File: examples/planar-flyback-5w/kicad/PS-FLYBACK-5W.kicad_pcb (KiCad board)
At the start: 6 copper layers, 50 x 104 mm, 29 parts, among them J1 18-36 V DC, J2 5 V / 1 A isolated, T1 PLANAR 4:2 / Lm 13.12uH, U1 LT8302IS8E#PBF

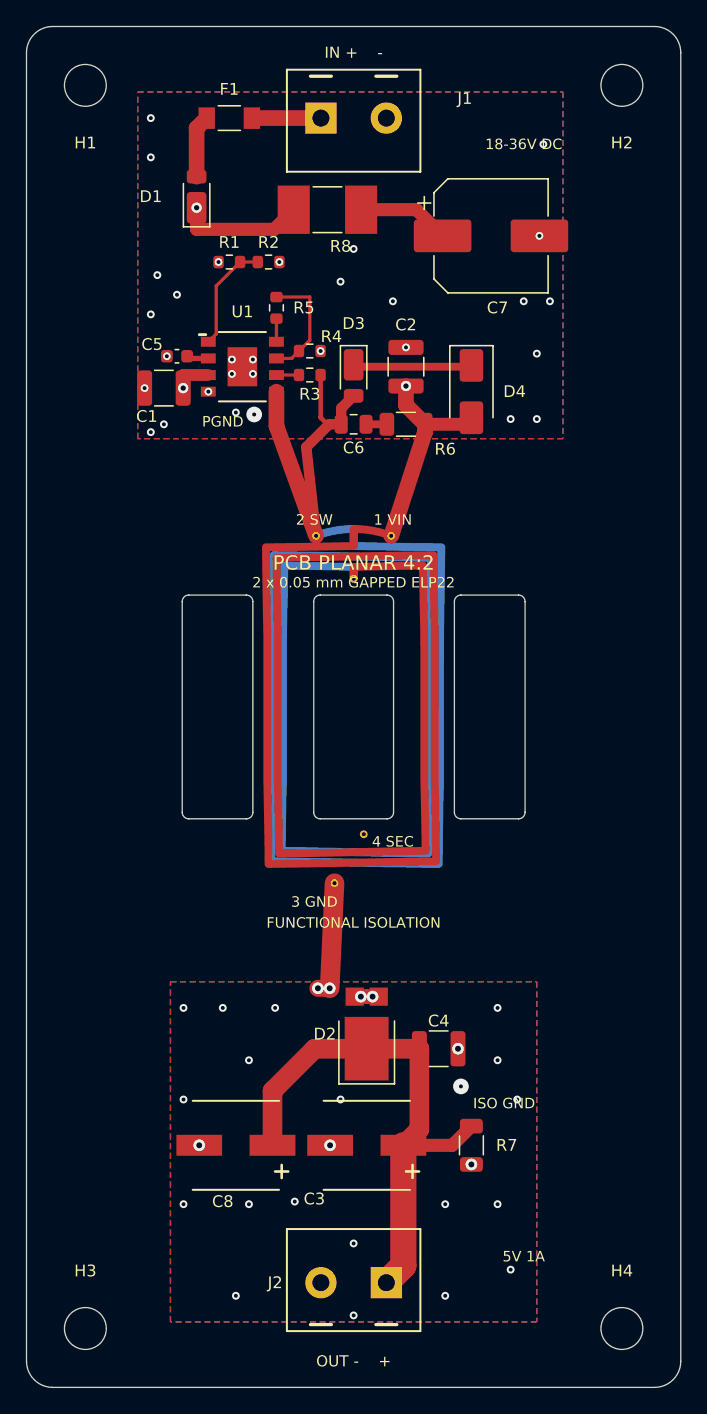
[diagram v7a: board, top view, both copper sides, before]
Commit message: Compact flyback A3 and verify TDK clip clearance
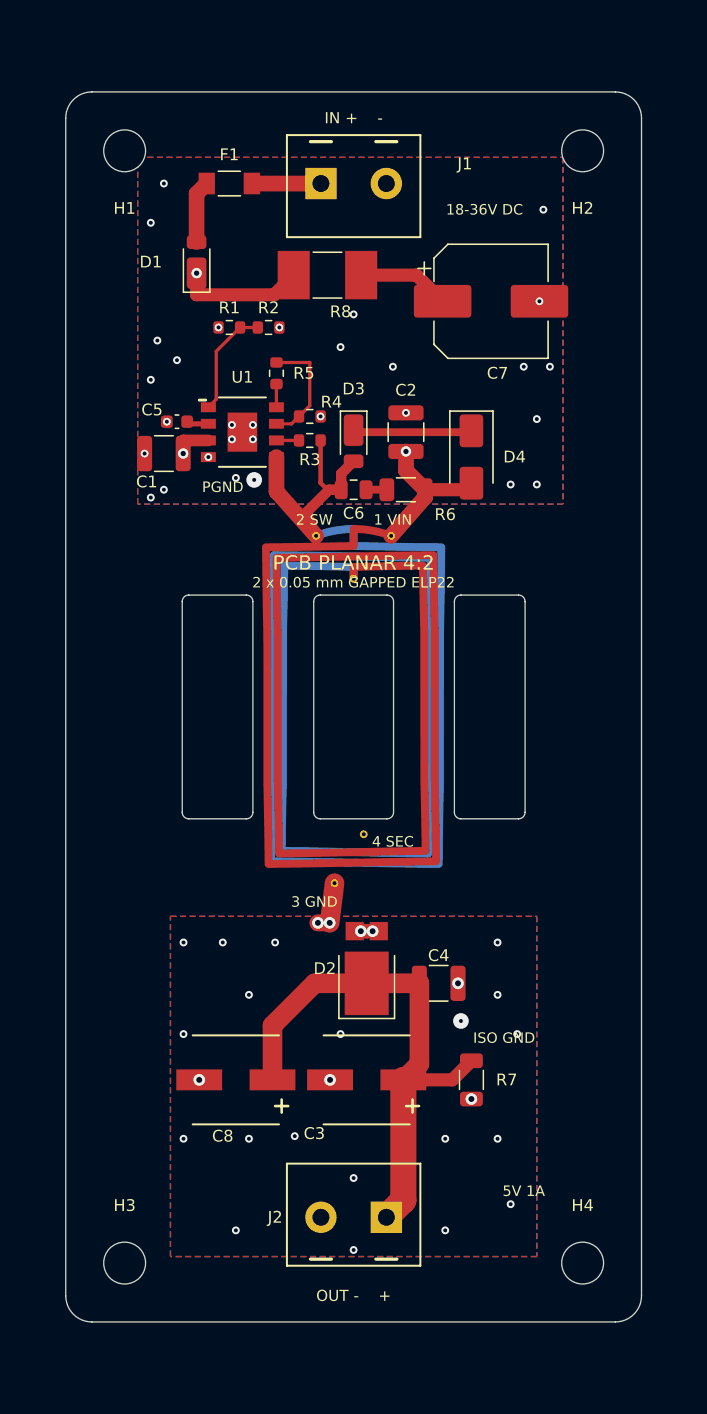
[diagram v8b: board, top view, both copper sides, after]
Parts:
- moved H1 5.83 mm to (82.5, 42.5)
- moved H2 5.83 mm to (117.5, 42.5)
- moved H3 5.83 mm to (82.5, 127.5)
- moved H4 5.83 mm to (117.5, 127.5)
- moved C1 5.00 mm to (85.5, 65.6)
- moved C6 5.00 mm to (100.0, 68.4)
- moved D4 5.00 mm to (109.0, 65.9)
- moved R3 5.00 mm to (96.7, 64.6)
- moved R6 5.00 mm to (104.0, 68.4)
- moved C2 5.00 mm to (104.0, 64.0)
- moved C3 5.00 mm to (101.0, 113.5)
- moved C4 5.00 mm to (106.5, 106.1)
- moved C5 5.00 mm to (86.5, 63.2)
- moved C7 5.00 mm to (110.5, 54.0)
- moved C8 5.00 mm to (91.0, 113.5)
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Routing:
- net /SW: track 28.4 -> 19.2 mm
- net /SEC_A: track 14.3 -> 9.29 mm
- net /GND_ISO: track 8.94 -> 3.96 mm
- net /VIN: track 65.6 -> 61.1 mm
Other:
- board size 50 x 104 mm -> 44 x 94 mm
- board text added: "A3 ENGINEERING PROTOTYPE"
- board text removed: "A2 ENGINEERING PROTOTYPE"
